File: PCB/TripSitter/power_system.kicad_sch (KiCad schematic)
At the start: 37 parts, among them J4 USB_B_Micro, J5 Jack-DC, SW2 SW_DPDT_x2, SW3 SW_DIP_x05, U2 TPS54325_PWP_14, U5 TPS54294PWP

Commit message: before
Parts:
- removed C60, C62, C75, C77: 22uF, Capacitor_SMD:C_0402_1005Metric_Pad0.74x0.62mm_HandSolder, symbol Device:C
- removed C64: 0.1uF, Capacitor_SMD:C_0201_0603Metric_Pad0.64x0.40mm_HandSolder, symbol Device:C
- removed C65, C67, C74: 10uF, Capacitor_SMD:C_0402_1005Metric_Pad0.74x0.62mm_HandSolder, symbol Device:C
- removed C66, C72, C73, C76: 100nF, Capacitor_SMD:C_0201_0603Metric_Pad0.64x0.40mm_HandSolder, symbol Device:C
- removed C68: 100n, Capacitor_SMD:C_0201_0603Metric_Pad0.64x0.40mm_HandSolder, symbol Device:C
- removed C70, C71: 1uF, Capacitor_SMD:C_0201_0603Metric_Pad0.64x0.40mm_HandSolder, symbol Device:C
- removed C78, C79: 22u, Capacitor_SMD:C_0402_1005Metric_Pad0.74x0.62mm_HandSolder, symbol Device:C
- removed R20: 30.1k, Resistor_SMD:R_0805_2012Metric_Pad1.20x1.40mm_HandSolder, symbol Device:R
- removed R21, R23, R27: 22.1k, Resistor_SMD:R_0805_2012Metric_Pad1.20x1.40mm_HandSolder, symbol Device:R
- removed R25: 100k, Resistor_SMD:R_0805_2012Metric_Pad1.20x1.40mm_HandSolder, symbol Device:R
- removed R26: 73.2k, Resistor_SMD:R_0805_2012Metric_Pad1.20x1.40mm_HandSolder, symbol Device:R
- removed SW3: SW_DIP_x05, Connector_PinHeader_1.27mm:PinHeader_2x05_P1.27mm_Vertical, symbol Switch:SW_DIP_x05
- added C803, C805, C811, C812, C815, C817: 0.1uF, Capacitor_SMD:C_0603_1608Metric_Pad1.08x0.95mm_HandSolder, symbol Device:C
- added C804, C810, C816: 10uF, Capacitor_SMD:C_0402_1005Metric_Pad0.74x0.62mm_HandSolder, symbol Device:C
- added C806, C807, C808, C809, C818, C819: 22uF, Capacitor_SMD:C_0603_1608Metric_Pad1.08x0.95mm_HandSolder, symbol Device:C
- added C813, C814: 1uF, Capacitor_SMD:C_0402_1005Metric_Pad0.74x0.62mm_HandSolder, symbol Device:C
- added J801: Conn_02x05_Odd_Even, Connector_PinHeader_2.00mm:PinHeader_2x05_P2.00mm_Vertical, symbol Connector_Generic:Conn_02x05_Odd_Even
- added R801: 30.1K, Resistor_SMD:R_0805_2012Metric_Pad1.20x1.40mm_HandSolder, symbol Device:R
- added R802, R803, R805: 22.1K, Resistor_SMD:R_0805_2012Metric_Pad1.20x1.40mm_HandSolder, symbol Device:R
- added R804: 100K, Resistor_SMD:R_0805_2012Metric_Pad1.20x1.40mm_HandSolder, symbol Device:R
- added R806: 73.2K, Resistor_SMD:R_0805_2012Metric_Pad1.20x1.40mm_HandSolder, symbol Device:R
- C69: footprint Capacitor_SMD:C_0402_1005Metric_Pad0.74x0.62mm_HandSolder -> Capacitor_SMD:C_0201_0603Metric_Pad0.64x0.40mm_HandSolder
- C801: renamed from C61; footprint Capacitor_SMD:C_1210_3225Metric_Pad1.33x2.70mm_HandSolder -> Capacitor_SMD:C_0805_2012Metric_Pad1.18x1.45mm_HandSolder; Component Name (none) -> CL21A107MQYNNWE; DK_Ref (none) -> https://www.digikey.no/en/products/detail/samsung-electro-m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
- C802: renamed from C63; Component Name (none) -> CL10A106KQ8NNNC; DK_Ref (none) -> https://www.digikey.no/en/products/detail/samsung-electro-m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
- R807: renamed from R24; Component Name (none) -> RR1220P-104-D; DK_Ref (none) -> https://www.digikey.no/product-detail/no/susumu/RR1220P-104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
- SW801: renamed from SW2; footprint Button_Switch_SMD:SW_DPDT_CK_JS202011JCQN -> Button_Switch_THT:SW_E-Switch_EG2219_DPDT_Angled
- renumbered J5 to J802, J4 to J803, L1 to L801, L2 to L802
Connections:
- net +1V0: now also J801.2 (Pin_2)
- net +1V5: now also J801.10 (Pin_10)
- net +1V8: now also J801.6 (Pin_6)
- net +3.3V: now also J801.8 (Pin_8)
- net +5V: now also J801.4 (Pin_4)
- net 1V0: now also C806.2, C807.2, J801.1 (Pin_1)
- net 1V5: now also C804.1, J801.9 (Pin_9)
- net 1V8: now also C808.2, C809.2, J801.5 (Pin_5), R801.1
- net 3V3: now also C818.2, C819.2, J801.7 (Pin_7), R806.1
- net 5V0: now also C803.1, C810.1, C811.2, C812.1, C816.1, C817.1, J801.3 (Pin_3)
- net GND: now also C803.2, C806.1, C807.1, C808.1, C809.1, C810.2, C812.2, C813.2, C814.2, C816.2, C817.2, C818.1, C819.1, R801.2, R802.1, R802.2, R803.2, R805.2
- net at U5.10 (VFB2): now also R805.1, R806.2
- net at L802.1, U2.10 (SW1), U2.11 (SW2): now also C805.1
- net at U2.12 (VBST): now also C805.2
- net at U5.15 (VBST2): now also C815.1
- net at L3.1, U5.14 (SW2): now also C815.2
- net at U5.12 (EN2), U5.6 (PG1): now also R804.2
- net at U5.2 (VBST1): now also C811.1
- net at U5.9 (VREG5): now also C814.1, R804.1
- net at R22.2, U2.2 (VFB): now also C804.2, R803.1
- net VBUS: now reaches J803.1 (VBUS), SW801.1 (A)
- net at R807.2, U2.3 (VREG5): now also C813.1
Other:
- note added: "FPGA boot sequence 3.3V > 1.8V > 1.5V > 1.0V"
- note added: "Is this value correct?"

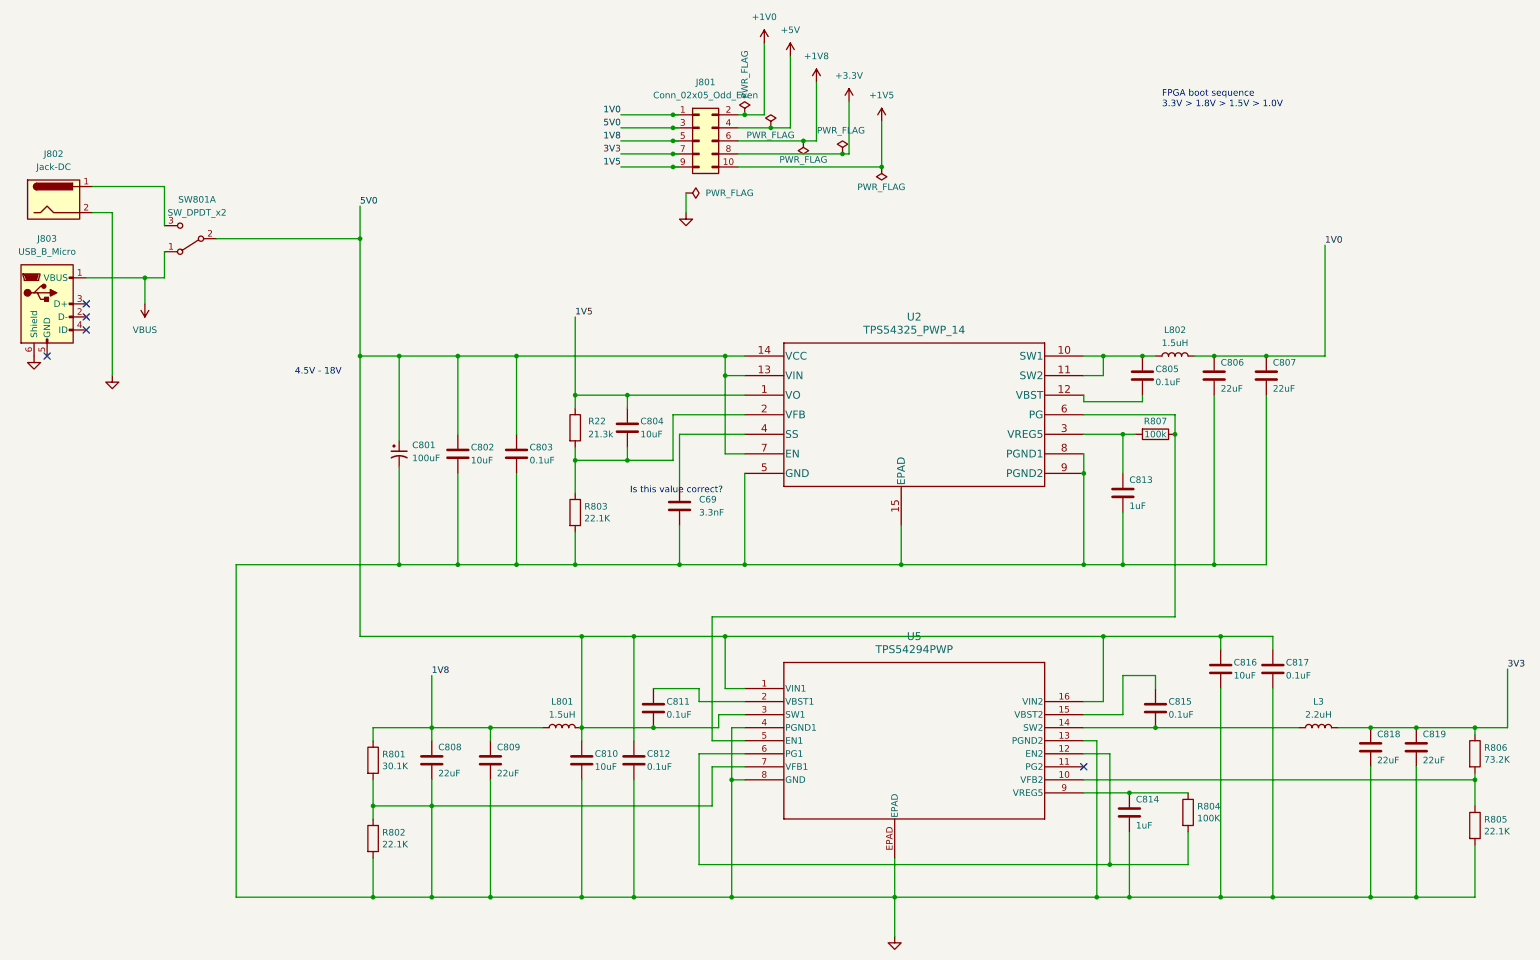
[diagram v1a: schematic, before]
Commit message: redo power circuit and add heat sink
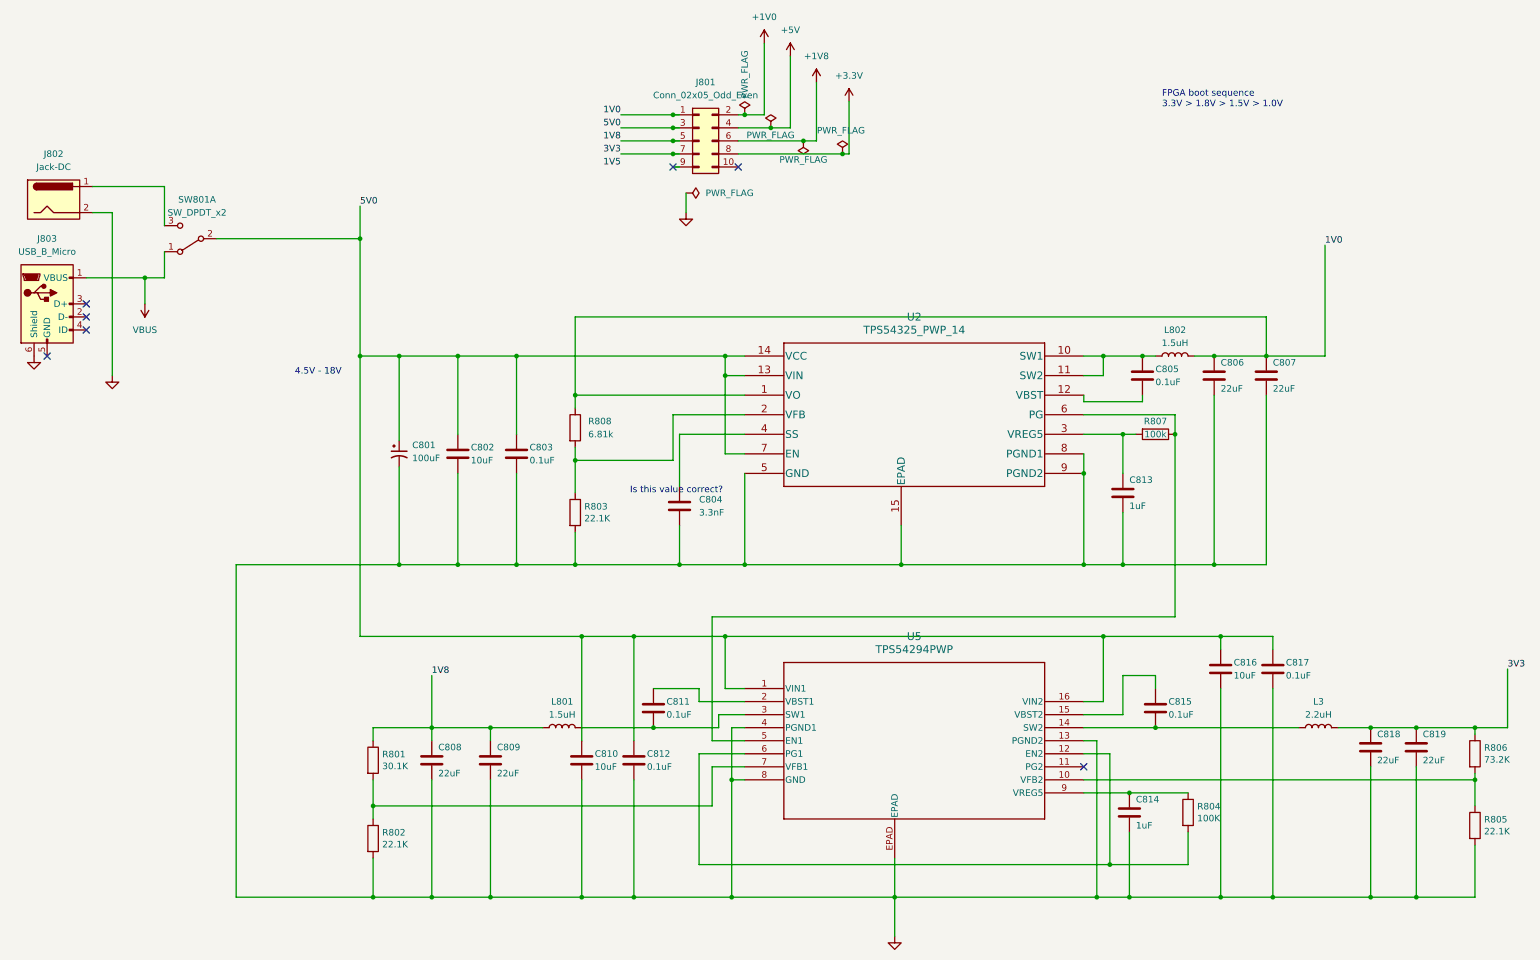
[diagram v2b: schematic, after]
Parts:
- removed C804: 10uF, Capacitor_SMD:C_0402_1005Metric_Pad0.74x0.62mm_HandSolder, symbol Device:C
- R808: renamed from R22; value 21.3k -> 6.81k
- renumbered C69 to C804
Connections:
- net 1V0: now also R808.1, U2.1 (VO)
- net 1V5: no longer J801.9 (Pin_9), R808.1, U2.1 (VO)
- net 5V0: no longer C811.2, L801.2, U5.3 (SW1)
- net GND: no longer R801.2, R802.1, U5.7 (VFB1)
- net +1V5: no longer names the net of J801.10 (Pin_10)
- new net: C811.2, L801.2, U5.3 (SW1)
- new net: R801.2, R802.1, U5.7 (VFB1)
- no-connect marks 5 -> 7

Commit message: pcb: Finalized routing without DDR3
Added ground and power plane, layed out all the components, fanned out
BGA. QSPI between FPGA->MCU->SRAM and MCU->SRAM is routed. Most is done
but DRC does not pass so do not produce.
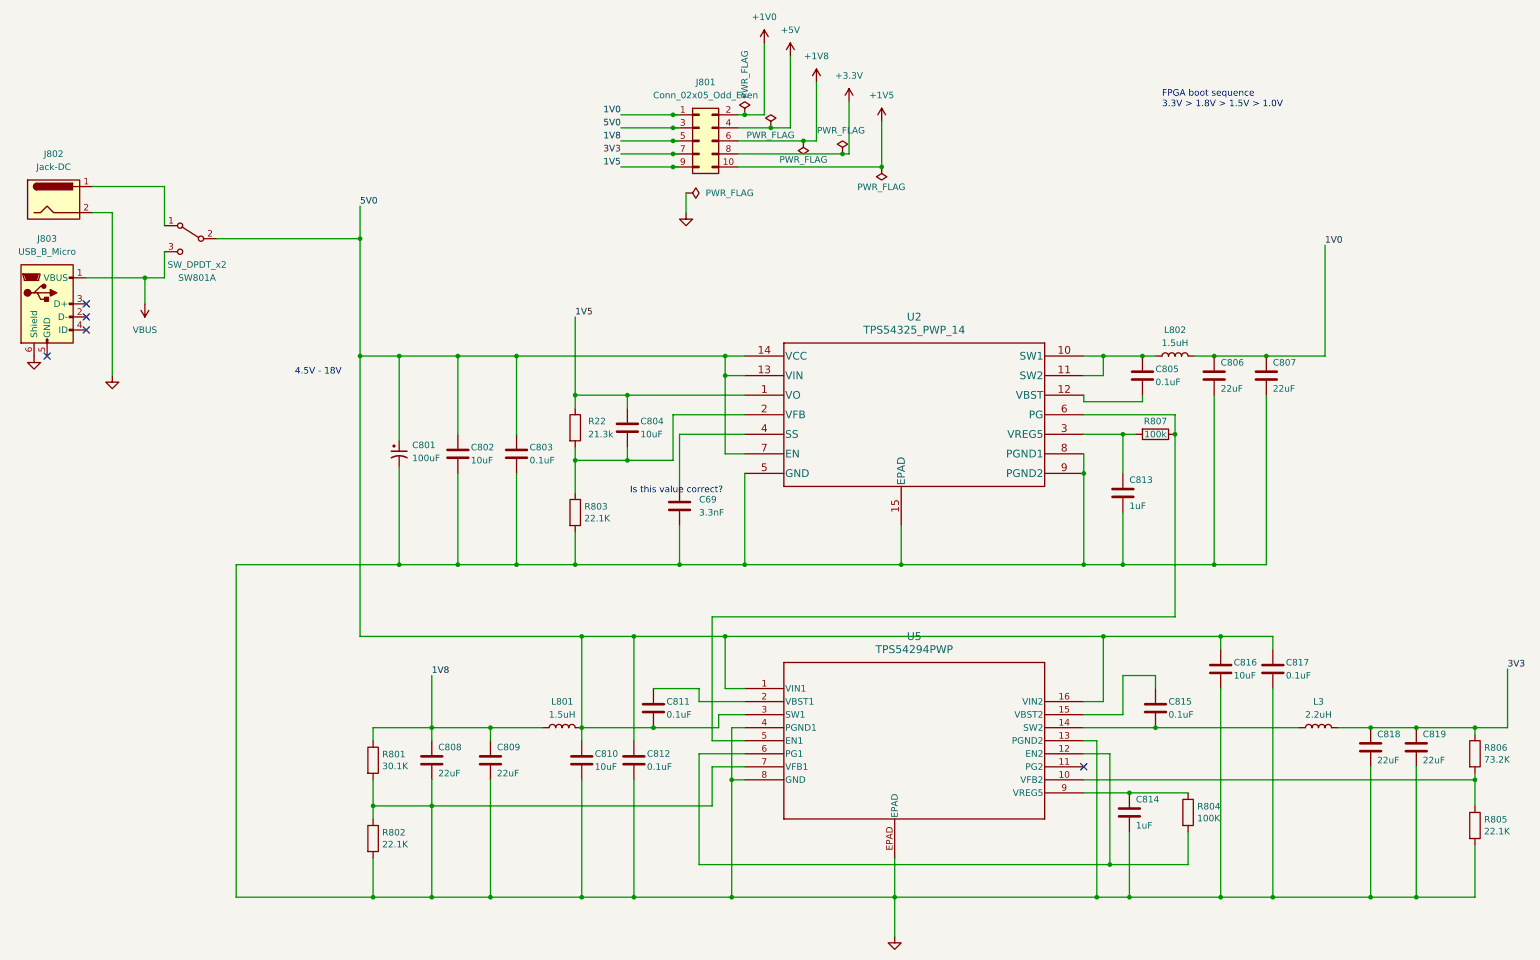
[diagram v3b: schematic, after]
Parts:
- added C804: 10uF, Capacitor_SMD:C_0402_1005Metric_Pad0.74x0.62mm_HandSolder, symbol Device:C
- R22: renamed from R808; value 6.81k -> 21.3k
- SW801: footprint Button_Switch_THT:SW_E-Switch_EG2219_DPDT_Angled -> Button_Switch_THT:SW_E-Switch_EG1224_SPDT_Angled
- renumbered C804 to C69
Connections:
- net 1V0: no longer R22.1, U2.1 (VO)
- net 1V5: now also J801.9 (Pin_9), R22.1, U2.1 (VO), C804.1
- net 5V0: now also C811.2, L801.2, U5.3 (SW1)
- net GND: now also R801.2, R802.1, U5.7 (VFB1)
- net VBUS: now also SW801.3 (C); no longer SW801.1 (A)
- net +1V5: now reaches J801.10 (Pin_10)
- net at J802.1: now also SW801.1 (A); no longer SW801.3 (C)
- net at R22.2, R803.1, U2.2 (VFB): now also C804.2
- no-connect marks 7 -> 5
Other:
- moved on the sheet: SW801A
